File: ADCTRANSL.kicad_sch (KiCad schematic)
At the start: 10 parts

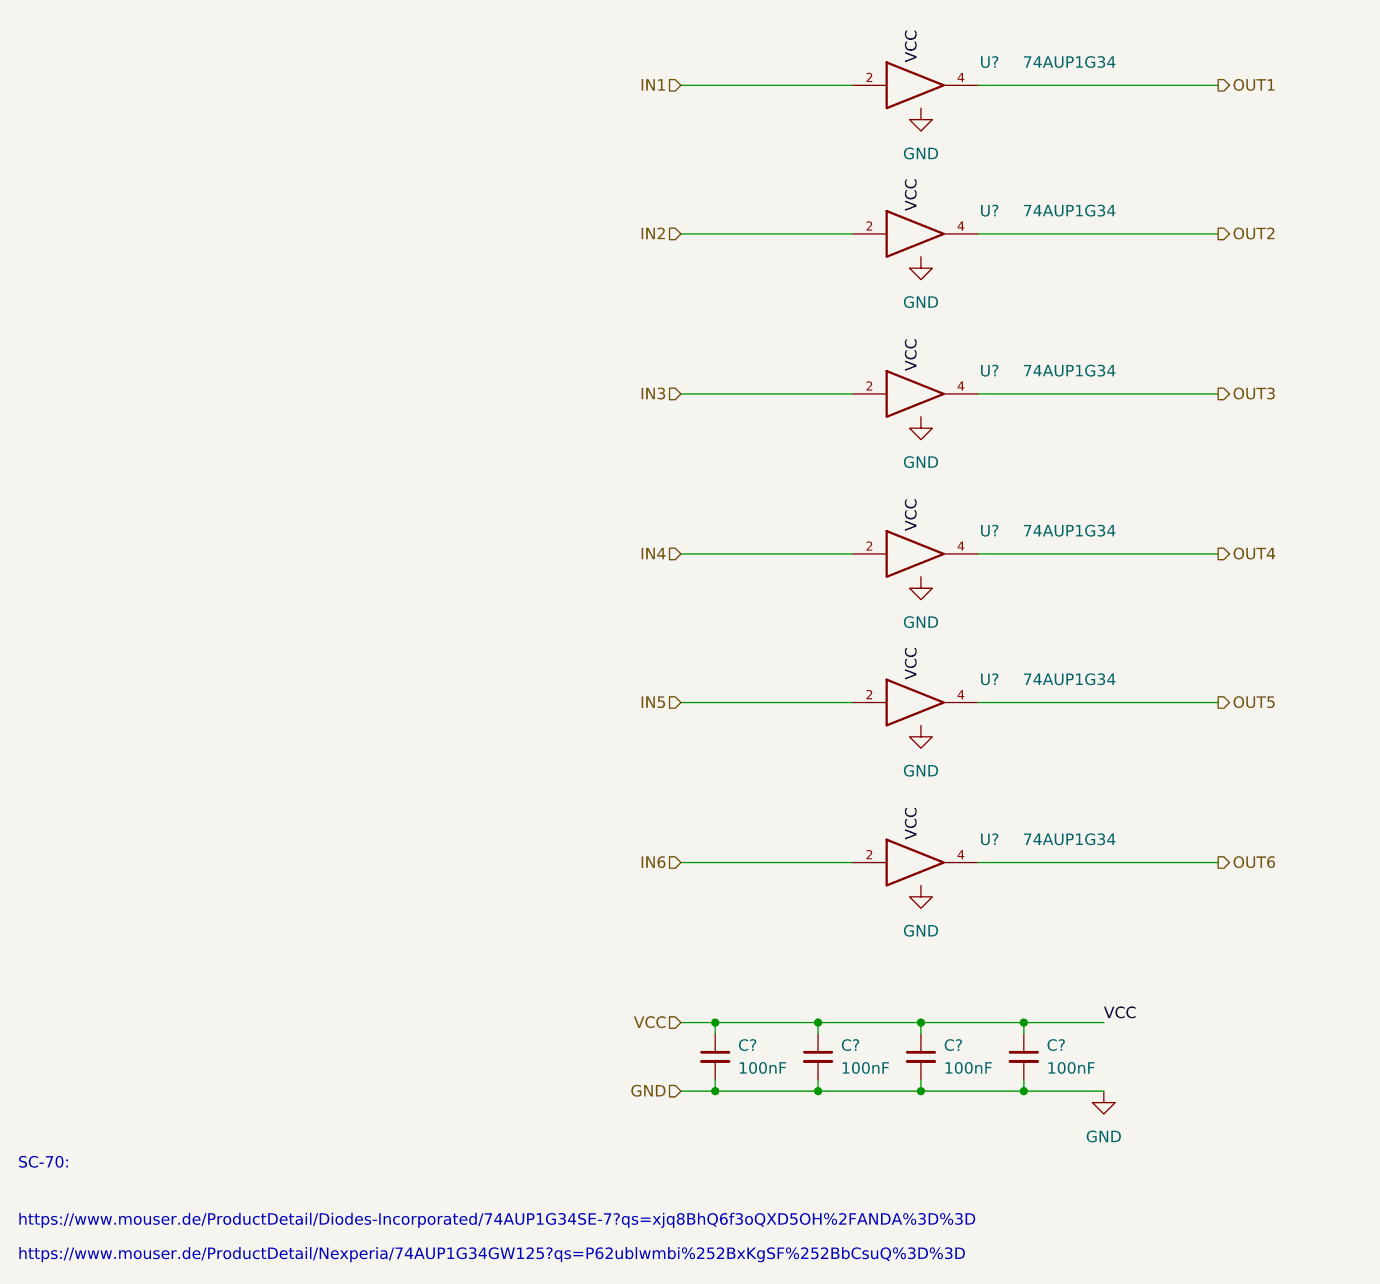
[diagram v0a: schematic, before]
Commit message: annotated and packages defined
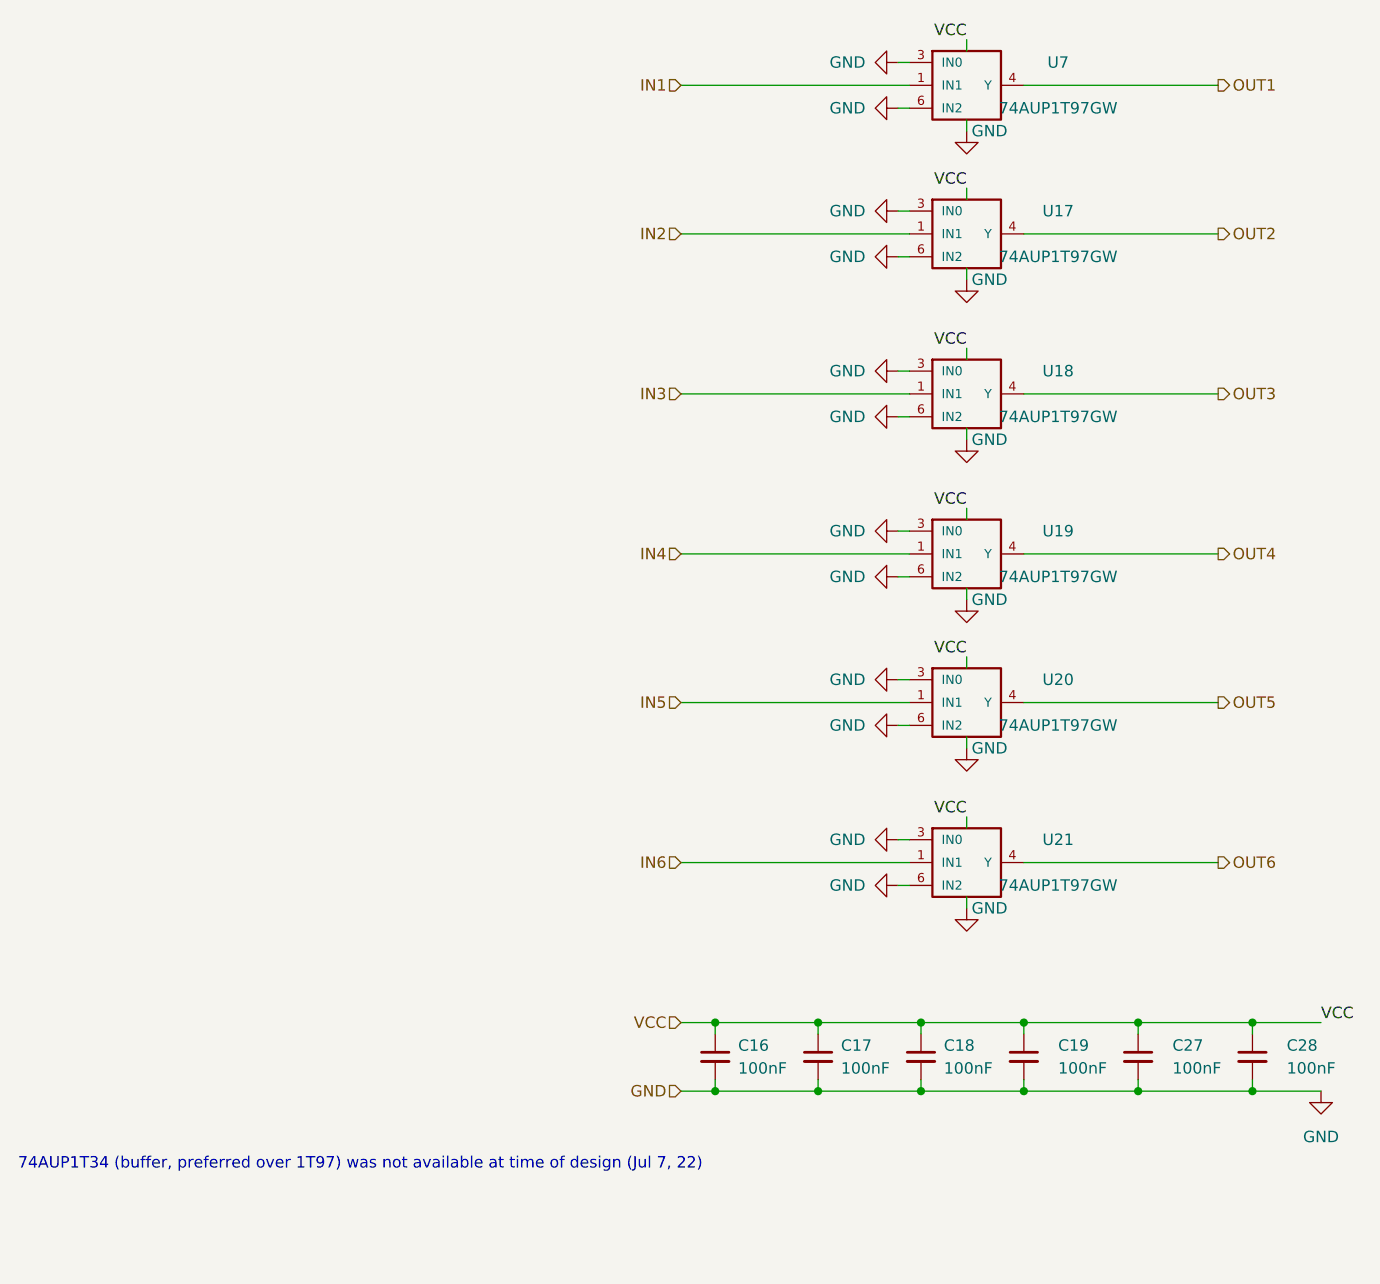
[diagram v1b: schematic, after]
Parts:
- removed U? (x6): 74AUP1G34, symbol 74xGxx:74AUP1G34
- added C27, C28: 100nF, Capacitor_SMD:C_0805_2012Metric, symbol Device:C_Small
- added U17, U18, U19, U20, U21, U7: 74AUP1T97GW, Package_TO_SOT_SMD:SOT-363_SC-70-6_Handsoldering, symbol 74xGxx:74AUP1G97
- C16, C17, C18, C19: renamed from C?; footprint (none) -> Capacitor_SMD:C_0805_2012Metric
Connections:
- net GND: now also C27.2, C28.2, U17.2 (GND), U17.3 (IN0), U17.6 (IN2), U18.2 (GND), U18.3 (IN0), U18.6 (IN2), U19.2 (GND), U19.3 (IN0), U19.6 (IN2), U20.2 (GND), U20.3 (IN0), U20.6 (IN2), U21.2 (GND), U21.3 (IN0), U21.6 (IN2), U7.2 (GND), U7.3 (IN0), U7.6 (IN2)
- net IN1: now also U7.1 (IN1)
- net IN2: now also U17.1 (IN1)
- net IN3: now also U18.1 (IN1)
- net IN4: now also U19.1 (IN1)
- net IN5: now also U20.1 (IN1)
- net IN6: now also U21.1 (IN1)
- net OUT1: now also U7.4 (Y)
- net OUT2: now also U17.4 (Y)
- net OUT3: now also U18.4 (Y)
- net OUT4: now also U19.4 (Y)
- net OUT5: now also U20.4 (Y)
- net OUT6: now also U21.4 (Y)
- net VCC: now also C27.1, C28.1, U17.5 (VCC), U18.5 (VCC), U19.5 (VCC), U20.5 (VCC), U21.5 (VCC), U7.5 (VCC)
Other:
- note added: "74AUP1T34 (buffer, preferred over 1T97) was not available at time of design (Jul 7, 22)"
- note removed: "SC-70:"
- note removed: "https://www.mouser.de/ProductDetail/Diodes-Incorporated/74AUP1G34SE-7?qs=xjq8BhQ6f3oQXD5OH%2FANDA%3D%3D"
- note removed: "https://www.mouser.de/ProductDetail/Nexperia/74AUP1G34GW125?qs=P62ublwmbi%252BxKgSF%252BbCsuQ%3D%3D"
- company: (none) -> papamidas DM1CR
- title: (none) -> H7DDCADC

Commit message: placement_in_progress 1
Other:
- note added: "NXP Suffix GW = TSSOP6 (SOT363-2, 0.65 mm pitch)"
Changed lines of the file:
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@@
+    (effects (font (size 1.27 1.27)) (justify left bottom))
+  )
+  (text "NXP Suffix GW = TSSOP6 (SOT363-2, 0.65 mm pitch)" (at 119.38 132.08 0)
     (effects (font (size 1.27 1.27)) (justify left bottom))
   )
